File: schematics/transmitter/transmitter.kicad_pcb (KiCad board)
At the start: 4 copper layers, 38 x 72.6 mm, 24 parts, among them Q1 2N7000, SW1 SW_Nidec_CAS-120A1, U1 PIC16F18324-xSL, U2 NRF24L01_Breakout, U3 LM2937xT

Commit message: Updated switch with better 3d model
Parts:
- removed H3: MountingHole_Pad, MountingHole:MountingHole_2.5mm_Pad_TopBottom
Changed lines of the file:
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@@
 			(pintype "passive")
 		)
-		(model "${KICAD8_3DMODEL_DIR}/Connector_PinSocket_2.54mm.3dshapes/PinSocket_1x03_P2.54mm_Vertical.wrl"
+		(model "${KIPRJMOD}/3d_models/switch v1.step"
 			(offset
-				(xyz 0 0 0)
+				(xyz 0 -2.5 0)
 			)
 			(scale
@@
 			)
 			(rotate
-				(xyz 0 0 0)
+				(xyz 0 0 -90)
 			)
 		)
@@
 		)
 	)
-	(footprint "MountingHole:MountingHole_2.5mm_Pad_TopBottom"
-		(layer "F.Cu")
-		(at 76 120)
-		(descr "Mounting Hole 2.5mm")
-		(tags "mounting hole 2.5mm")
-		(property "Reference" "H3"
-			(at 0 -3.5 0)
-			(layer "F.SilkS")
-			(hide yes)
-			(effects
-				(font
-					(size 1 1)
-					(thickness 0.15)
-				)
-			)
-		)
-		(property "Value" "MountingHole_Pad"
-			(at 0 3.5 0)
-			(layer "F.Fab")
-			(hide yes)
-			(effects
-				(font
-					(size 1 1)
-					(thickness 0.15)
-				)
-			)
-		)
-		(property "Footprint" "MountingHole:MountingHole_2.5mm_Pad_TopBottom"
-			(at 0 0 0)
-			(unlocked yes)
-			(layer "F.Fab")
-			(hide yes)
-			(effects
-				(font
-					(size 1.27 1.27)
-					(thickness 0.15)
-				)
-			)
-		)
-		(property "Datasheet" ""
-			(at 0 0 0)
-			(unlocked yes)
-			(layer "F.Fab")
-			(hide yes)
-			(effects
-				(font
-					(size 1.27 1.27)
-					(thickness 0.15)
-				)
-			)
-		)
-		(property "Description" "Mounting Hole with connection"
-			(at 0 0 0)
-			(unlocked yes)
-			(layer "F.Fab")
-			(hide yes)
-			(effects
-				(font
-					(size 1.27 1.27)
-					(thickness 0.15)
-				)
-			)
-		)
-		(property "Mfn" ""
-			(at 0 0 0)
-			(unlocked yes)
-			(layer "F.Fab")
-			(hide yes)
-			(effects
-				(font
-					(size 1 1)
-					(thickness 0.15)
-				)
-			)
-		)
-		(property "Mfn PN" ""
-			(at 0 0 0)
-			(unlocked yes)
-			(layer "F.Fab")
-			(hide yes)
-			(effects
-				(font
-					(size 1 1)
-					(thickness 0.15)
-				)
-			)
-		)
-		(property "Supplier" ""
-			(at 0 0 0)
-			(unlocked yes)
-			(layer "F.Fab")
-			(hide yes)
-			(effects
-				(font
-					(size 1 1)
-					(thickness 0.15)
-				)
-			)
-		)
-		(property "Supplier PN" ""
-			(at 0 0 0)
-			(unlocked yes)
-			(layer "F.Fab")
-			(hide yes)
-			(effects
-				(font
-					(size 1 1)
-					(thickness 0.15)
-				)
-			)
-		)
-		(property ki_fp_filters "MountingHole*Pad*")
-		(sheetname "Root")
-		(sheetfile "transmitter.kicad_sch")
-		(attr exclude_from_pos_files exclude_from_bom)
-		(fp_circle
-			(center 0 0)
-			(end 2.5 0)
-			(stroke
-				(width 0.15)
-				(type solid)
-			)
-			(fill none)
-			(layer "Cmts.User")
-		)
-		(fp_circle
-			(center 0 0)
-			(end 2.75 0)
-			(stroke
-				(width 0.05)
-				(type solid)
-			)
-			(fill none)
-			(layer "F.CrtYd")
-		)
-		(fp_text user "${REFERENCE}"
-			(at 0 0 0)
-			(layer "F.Fab")
-			(effects
-				(font
-					(size 1 1)
-					(thickness 0.15)
-				)
-			)
-		)
-		(pad "1" thru_hole circle
-			(at 0 0)
-			(size 2.9 2.9)
-			(drill 2.5)
-			(layers "*.Cu" "*.Mask")
-			(remove_unused_layers no)
-			(net 2 "GND")
-			(pinfunction "1")
-			(pintype "input")
-		)
-		(pad "1" connect circle
-			(at 0 0)
-			(size 5 5)
-			(layers "F.Cu" "F.Mask")
-			(net 2 "GND")
-			(pinfunction "1")
-			(pintype "input")
-		)
-		(pad "1" connect circle
-			(at 0 0)
-			(size 5 5)
-			(layers "B.Cu" "B.Mask")
-			(net 2 "GND")
-			(pinfunction "1")
-			(pintype "input")
-		)
-	)

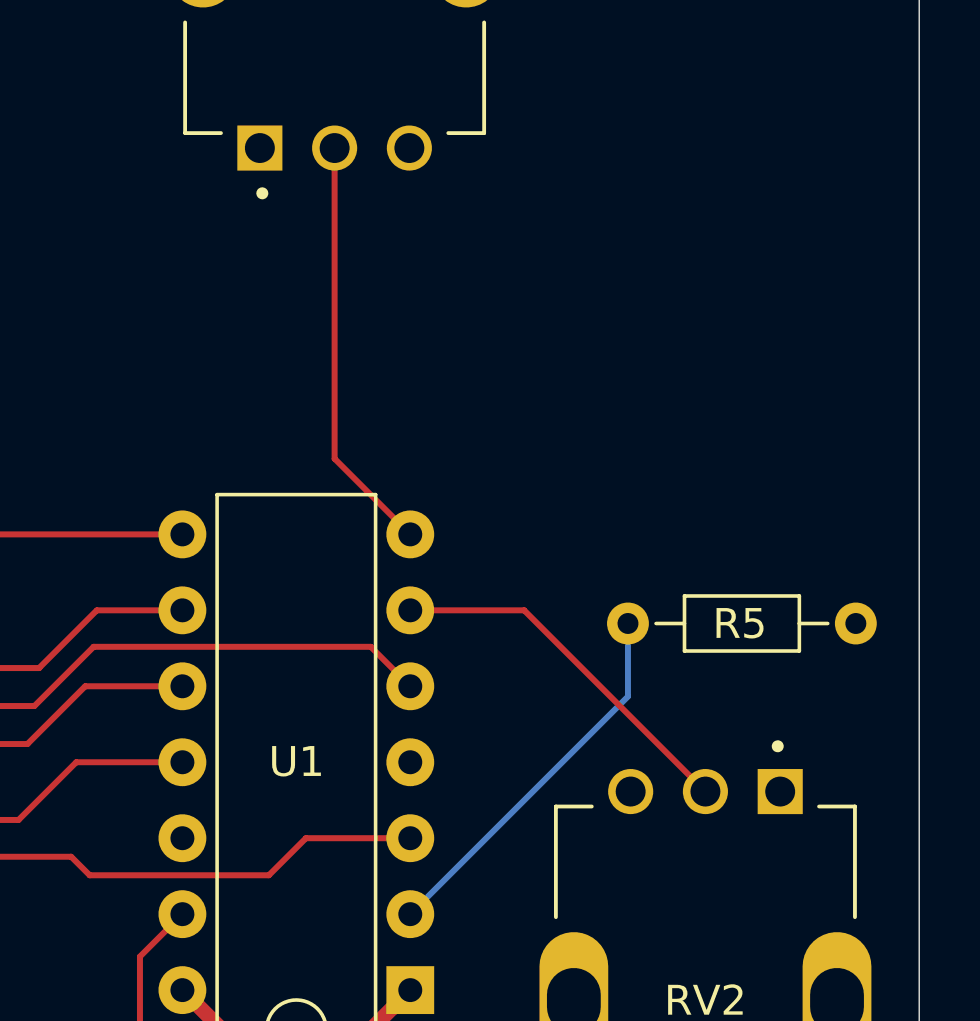
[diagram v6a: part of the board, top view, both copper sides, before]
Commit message: Add trim pot to transmitter
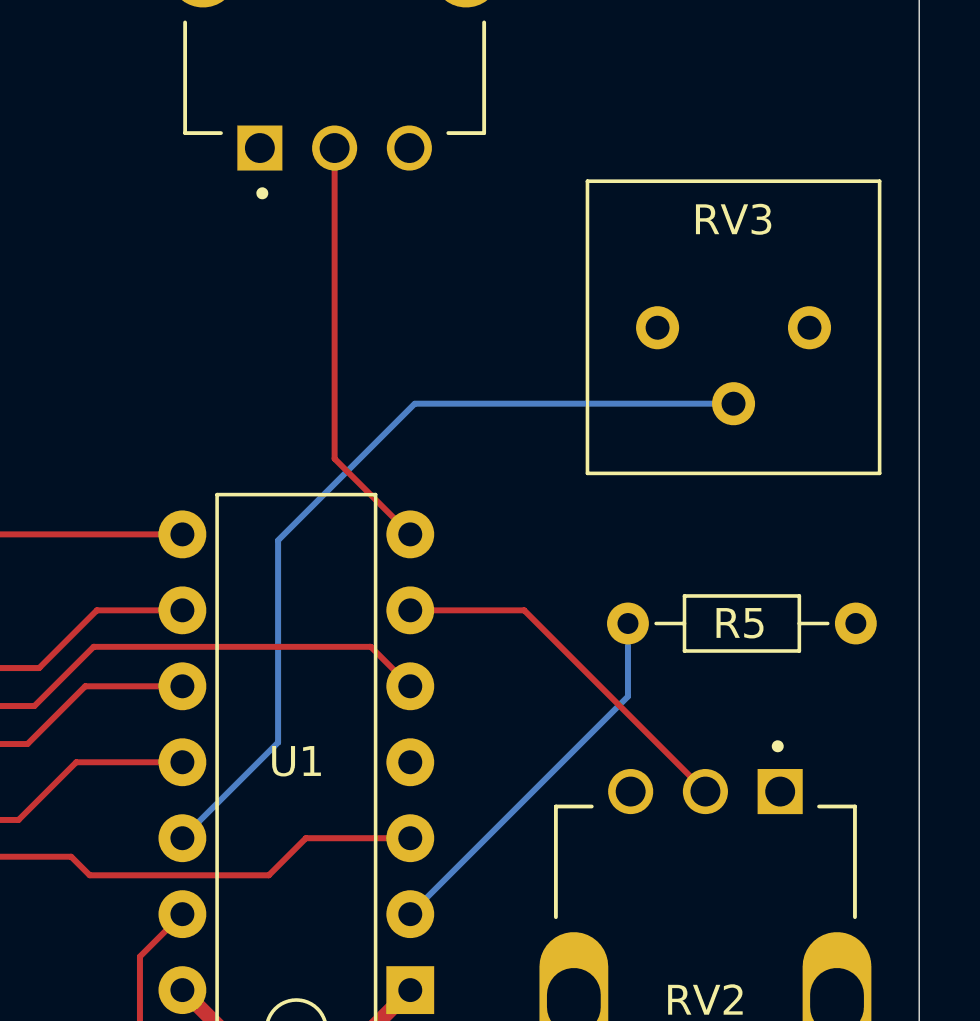
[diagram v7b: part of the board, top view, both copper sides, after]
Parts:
- added RV3: R_Potentiometer, Potentiometer_THT:Potentiometer_Bourns_3386P_Vertical, F.Cu at (102.2, 69.7)
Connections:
- C3 pad 1: unconnected-(C3-Pad1) -> +3.3V
- U1 pad 12: unconnected-(U1-RA1-Pad12) -> TRIM
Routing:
- net TRIM: track 0.00 -> 28.4 mm
